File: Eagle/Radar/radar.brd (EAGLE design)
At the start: 50.8 x 106.7 mm, 81 parts, among them IC4 MAX414ESD, X1 STEREOJACK, X2 BU-SMA-G, X3 BU-SMA-G, X4 BU-SMA-G

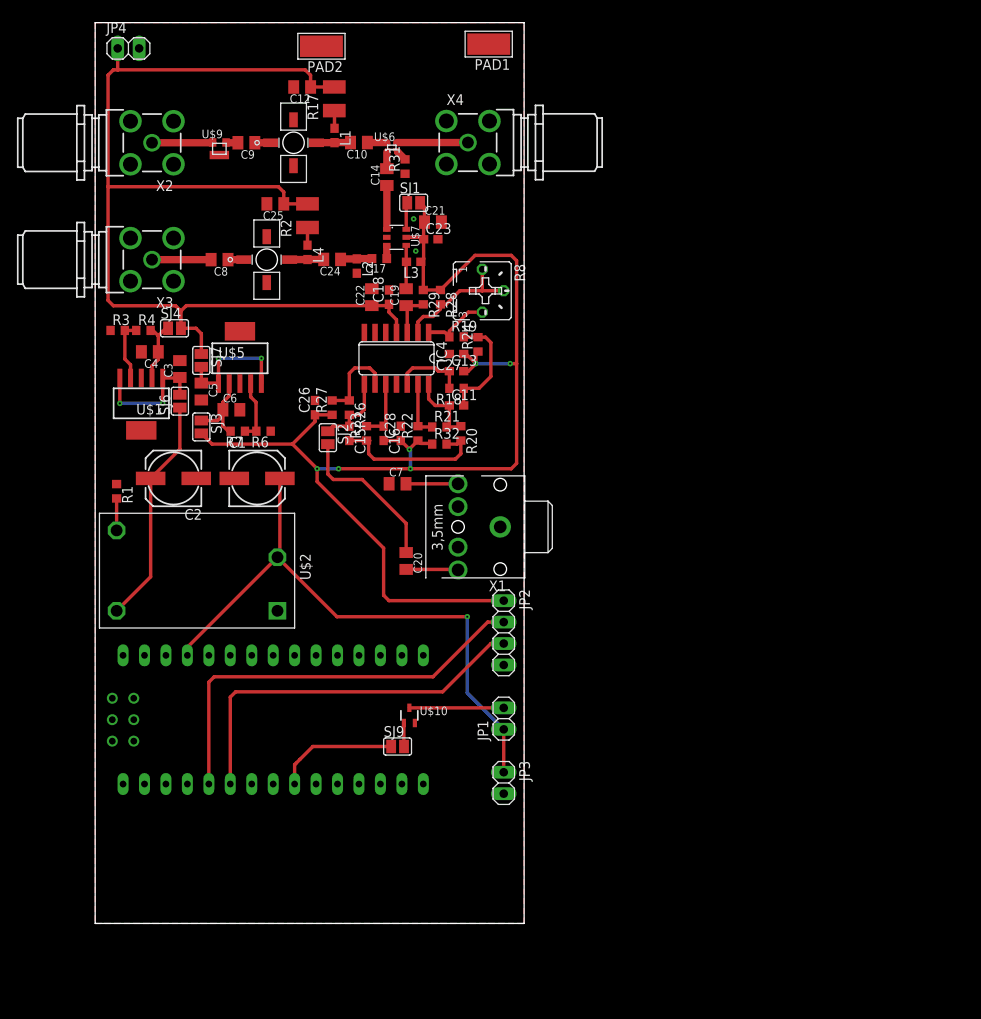
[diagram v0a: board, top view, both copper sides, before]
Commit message: Routes complete, no drc errors, no erc errors, need silks
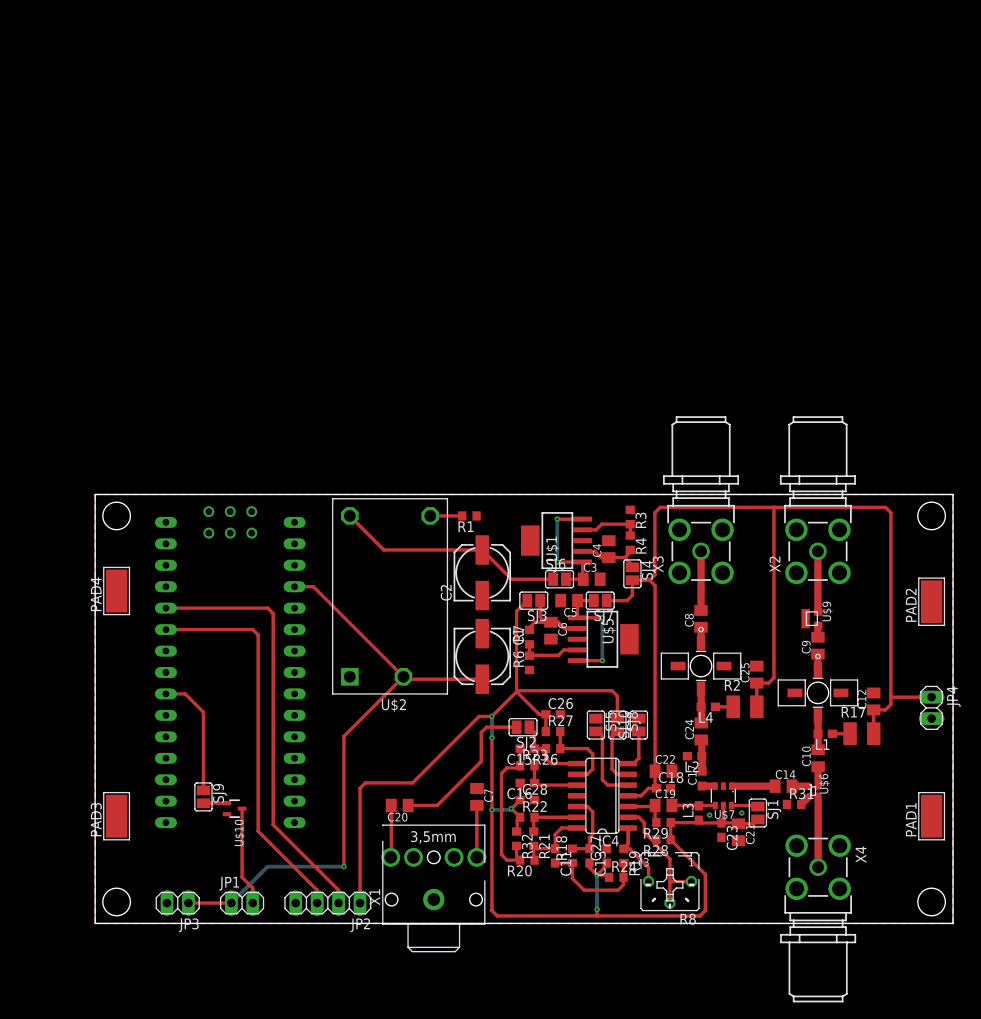
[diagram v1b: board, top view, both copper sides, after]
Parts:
- added PAD3, PAD4: WIREPADSMD5-2,5, wirepad:5-2,5
- added SJ10, SJ5, SJ8: (no value), jumper:SJ
- moved JP4 123.1 mm to (99.1, 25.5), turned to 270 degrees
- moved PAD1 105.4 mm to (99.1, 12.7), turned to 0 degrees
- moved C12 99.4 mm to (92.2, 26.3), turned to 90 degrees
- moved R17 97.8 mm to (90.8, 22.5), turned to 0 degrees
- moved PAD2 97.7 mm to (99.1, 38.1), turned to 0 degrees
- moved X4 95.3 mm to (85.6, 6.65), turned to 270 degrees
- moved X2 92.5 mm to (85.6, 44.1), turned to 90 degrees
- moved L1 91.6 mm to (86.5, 22.5), turned to 180 degrees
- moved U$6 91.1 mm to (85.1, 15.7), turned to 270 degrees
- moved C10 91.0 mm to (85.6, 19.6), turned to 90 degrees
- moved C9 90.2 mm to (85.6, 32.9), turned to 90 degrees
- moved U$8 90.0 mm to (85.6, 27.3), turned to 180 degrees
- moved U$9 89.2 mm to (84.6, 36.1), turned to 270 degrees
- moved R31 88.5 mm to (82.8, 14.1), turned to 0 degrees
- moved C14 86.1 mm to (81.5, 16.3), turned to 0 degrees
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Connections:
- new net N$2: IC4.7, SJ10.1
- new net N$4: IC4.5, SJ5.2
- new net N$5: IC4.6, SJ8.2
- net GND: now also PAD3.1, PAD4.1, SJ5.1
- net PP5V: now also SJ8.1
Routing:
- net PP5V: track 148.0 -> 162.9 mm
- net N$4: track 0.00 -> 9.37 mm
- net N$5: track 0.00 -> 6.90 mm
- net N$2: track 0.00 -> 4.68 mm
- net PP10V: track 128.2 -> 130.6 mm
- net PPUSB: track 71.1 -> 72.4 mm
- net MOTOR_CTRL: track 15.6 -> 14.6 mm
- net ENCODER_B: track 45.3 -> 45.8 mm
- net ENCODER_A: track 49.9 -> 50.5 mm
- net N$1: track 11.2 -> 11.7 mm
- added copper zone on layer 16, net GND
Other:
- board size 50.8 x 106.7 mm -> 101.6 x 50.8 mm

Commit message: Started silks, gnd stitch complete
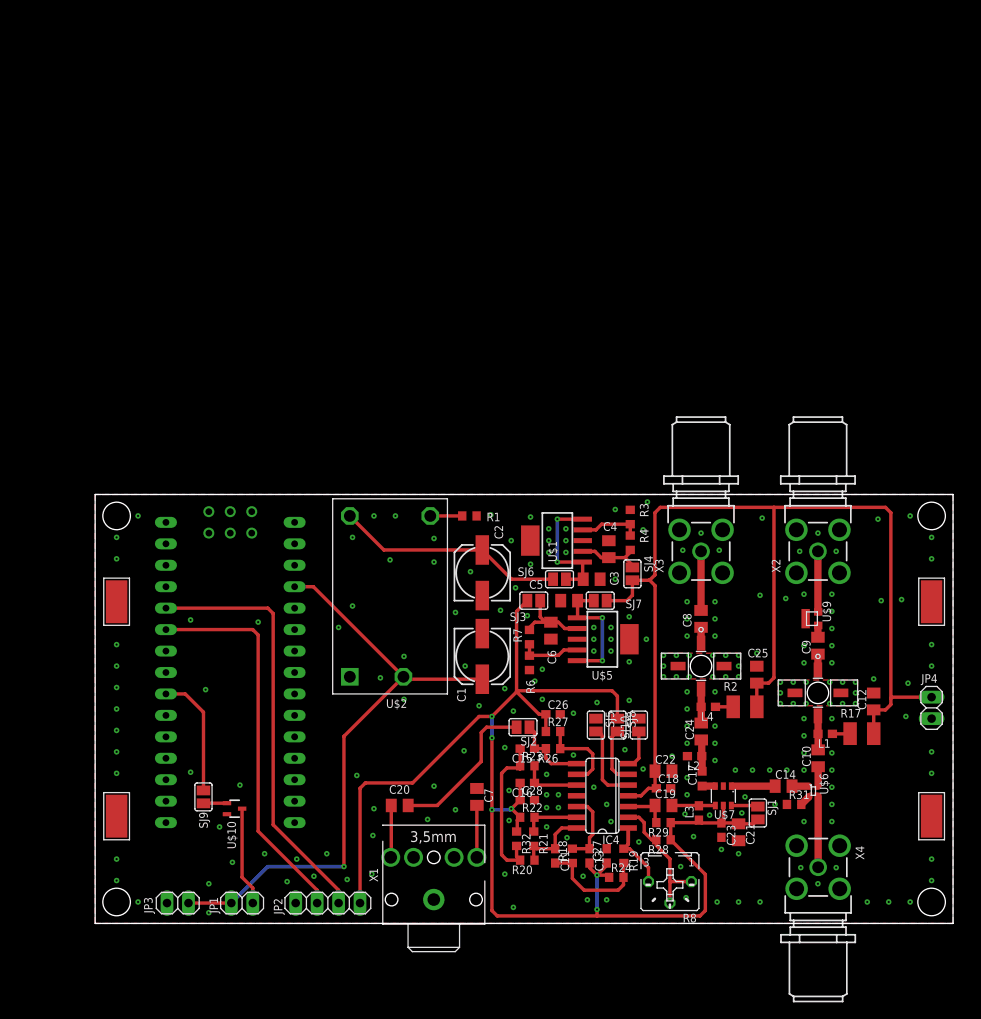
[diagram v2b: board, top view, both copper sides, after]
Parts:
- moved PAD4 1.27 mm to (2.54, 38.1)

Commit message: Design complete
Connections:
- net N$3 renamed RF__RX_IN
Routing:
- net PPUSB: track 72.4 -> 80.5 mm, vias 1 -> 4
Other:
- board text added: "A"
- board text added: "B"
- board text added: "ENCODER"
- board text added: "FMCW/Doppler Radar f: 2.4 - 2.5 GHz Justin Ng February 20, 2017 Cal Poly San Luis Obispo, CA"
- board text added: "GND"
- board text added: "Group 1b Nicholas Benitez Jacobe Labog Justin Ng Christi Tain Alex Wargo"
- board text added: "M+"
- board text added: "M-"
- board text added: "MOTOR"
- board text added: "PLL IN"
- board text added: "PLL POWER"
- board text added: "PP10V"
- board text added: "PP5V"
- board text added: "PPUSB"
- board text added: "RX ANT"
- board text added: "TX ANT"
